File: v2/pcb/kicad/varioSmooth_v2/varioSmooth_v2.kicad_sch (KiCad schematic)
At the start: 1 part, among them U1 MDBT50Q-1MV2

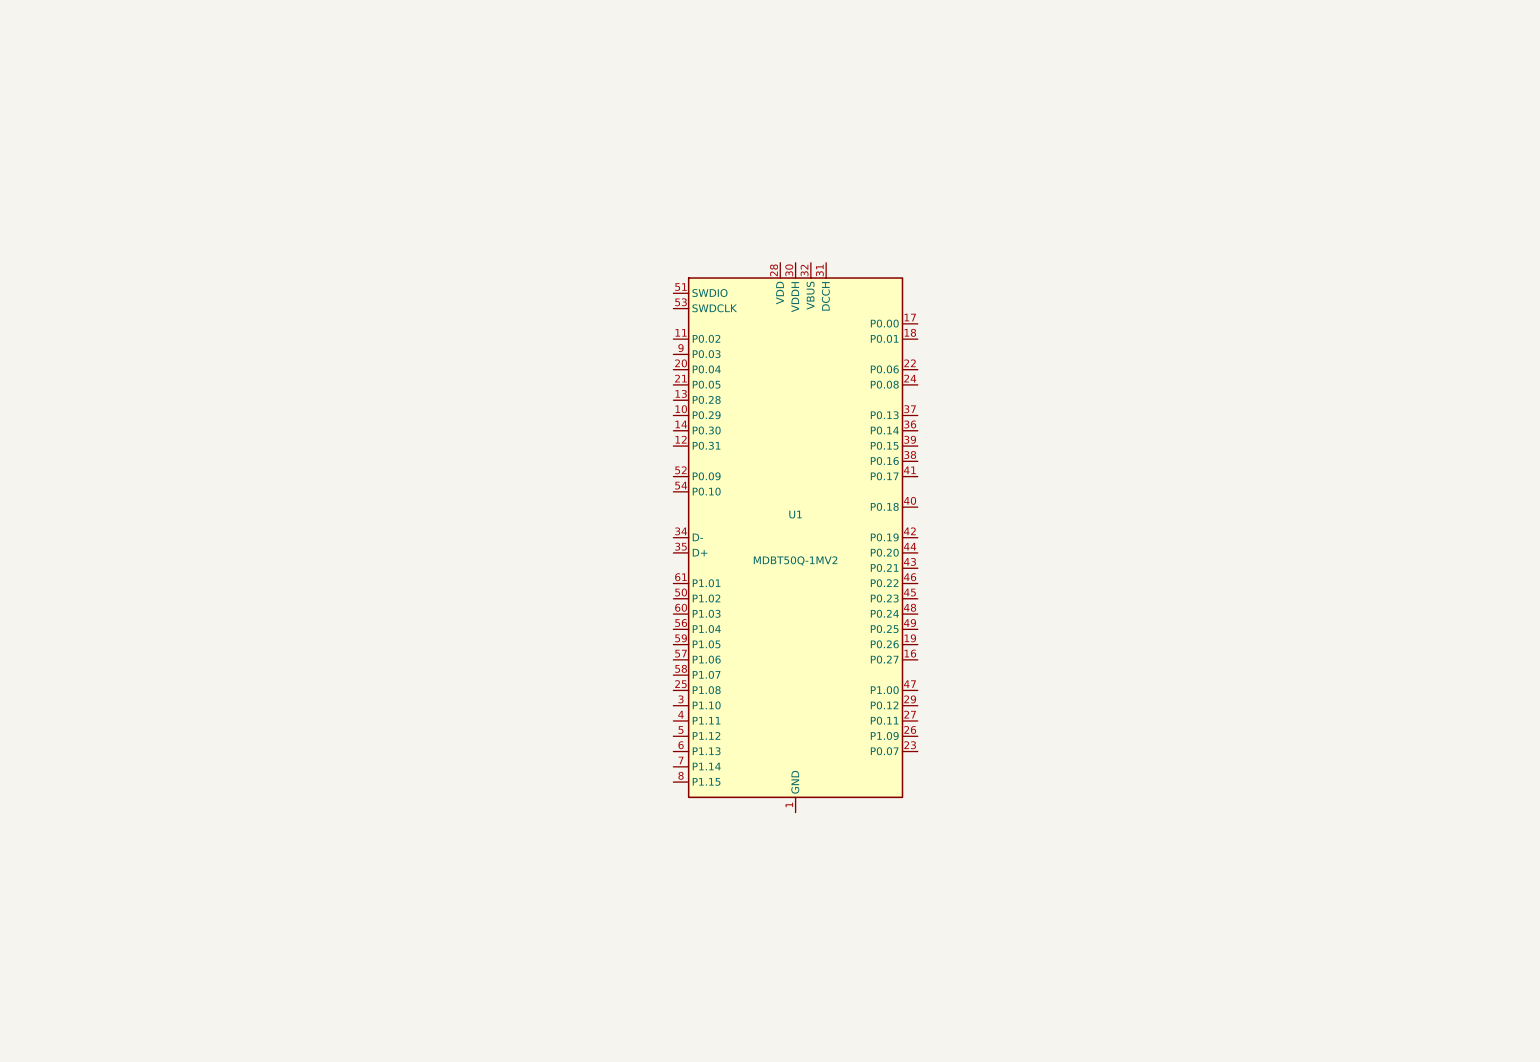
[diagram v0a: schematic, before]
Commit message: Draw the v2 schematic: power, USB, sensor, audio and debug
  LTC4071 shunt charger fed by the solar cells and by USB VBUS through
  Schottky diodes; MDBT50Q in high voltage mode (VDDH from the battery,
  REG0 DC/DC to a 3.3 V VDD). USB-C with CC pull-downs and USBLC6 ESD
  protection, MS5611 on I2C, piezo, button and 32 kHz crystal on the
  Feather pins so the firmware is unchanged, SWD and reset test pads.
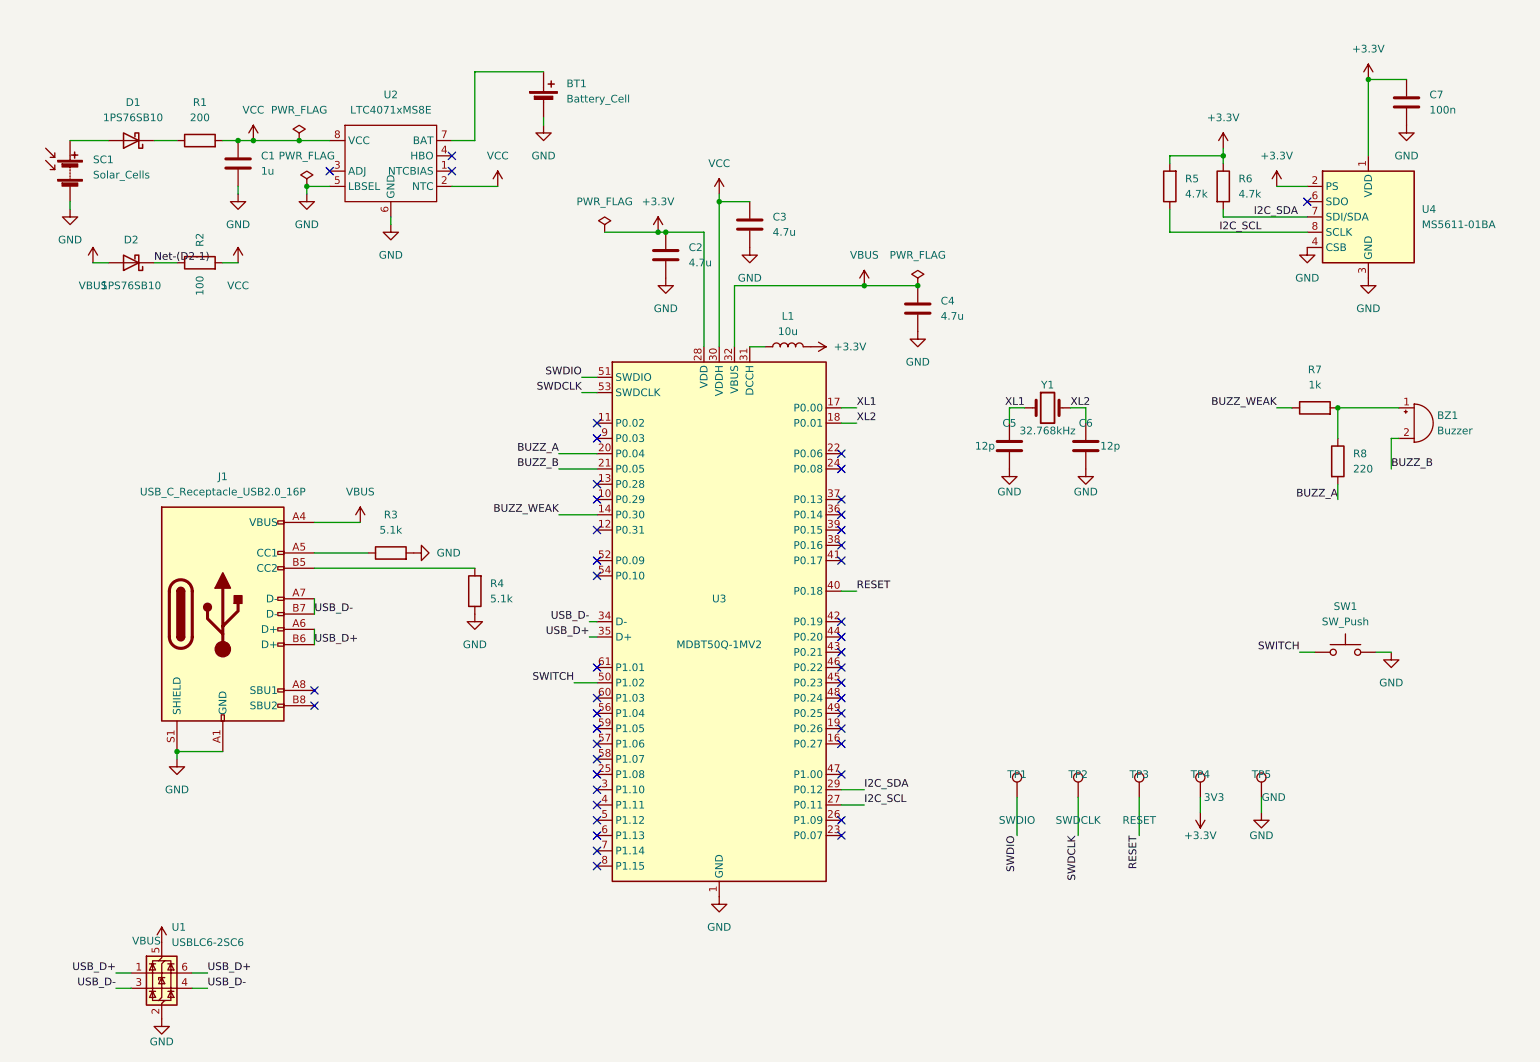
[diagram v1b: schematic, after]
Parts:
- added BT1: Battery_Cell, symbol Device:Battery_Cell
- added BZ1: Buzzer, symbol Device:Buzzer
- added C1: 1u, Capacitor_SMD:C_0603_1608Metric, symbol Device:C
- added C2, C3, C4: 4.7u, Capacitor_SMD:C_0603_1608Metric, symbol Device:C
- added C5, C6: 12p, Capacitor_SMD:C_0603_1608Metric, symbol Device:C
- added C7: 100n, Capacitor_SMD:C_0603_1608Metric, symbol Device:C
- added D1, D2: 1PS76SB10, Diode_SMD:D_SOD-323, symbol Device:D_Schottky
- added J1: USB_C_Receptacle_USB2.0_16P, Connector_USB:USB_C_Receptacle_GCT_USB4105-xx-A_16P_TopMnt_Horizontal, symbol Connector:USB_C_Receptacle_USB2.0_16P
- added L1: 10u, Inductor_SMD:L_0603_1608Metric, symbol Device:L
- added R1: 200, Resistor_SMD:R_0603_1608Metric, symbol Device:R
- added R2: 100, Resistor_SMD:R_0603_1608Metric, symbol Device:R
- added R3, R4: 5.1k, Resistor_SMD:R_0603_1608Metric, symbol Device:R
- added R5, R6: 4.7k, Resistor_SMD:R_0603_1608Metric, symbol Device:R
- added R7: 1k, Resistor_SMD:R_0603_1608Metric, symbol Device:R
- added R8: 220, Resistor_SMD:R_0603_1608Metric, symbol Device:R
- added SC1: Solar_Cells, symbol Device:Solar_Cells
- added SW1: SW_Push, symbol Switch:SW_Push
- added TP1: SWDIO, TestPoint:TestPoint_Pad_D1.5mm, symbol Connector:TestPoint
- added TP2: SWDCLK, TestPoint:TestPoint_Pad_D1.5mm, symbol Connector:TestPoint
- added TP3: RESET, TestPoint:TestPoint_Pad_D1.5mm, symbol Connector:TestPoint
- added TP4: 3V3, TestPoint:TestPoint_Pad_D1.5mm, symbol Connector:TestPoint
- added TP5: GND, TestPoint:TestPoint_Pad_D1.5mm, symbol Connector:TestPoint
- added U1: USBLC6-2SC6, Package_TO_SOT_SMD:SOT-23-6, symbol Power_Protection:USBLC6-2SC6
- added U2: LTC4071xMS8E, Package_SO:MSOP-8-1EP_3x3mm_P0.65mm_EP1.68x1.88mm, symbol varioSmooth_v2:LTC4071xMS8E
- added U4: MS5611-01BA, Package_LGA:LGA-8_3x5mm_P1.25mm, symbol Sensor_Pressure:MS5611-01BA
- added Y1: 32.768kHz, Crystal:Crystal_SMD_3215-2Pin_3.2x1.5mm, symbol Device:Crystal
- renumbered U1 to U3
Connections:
- net GND: now reaches U3.1 (GND), U3.15 (GND), U3.2 (GND), U3.33 (GND), U3.55 (GND)
- net GND: now also BT1.2 (-), C1.2, C2.2, C3.2, C4.2, C5.2, C6.2, C7.2, J1.A1 (GND), J1.A12 (GND), J1.B1 (GND), J1.B12 (GND), J1.S1 (SHIELD), R3.2, R4.1, SC1.2 (-), SW1.2, TP5.1, U1.2 (GND), U2.5 (LBSEL), U2.6 (GND), U2.9 (GND), U4.3 (GND), U4.4 (CSB), U4.5 (CSB)
- net BUZZ_WEAK: now reaches U3.14 (P0.30)
- net BUZZ_WEAK: now also R7.1
- net XL1: now reaches U3.17 (P0.00)
- net XL1: now also C5.1, Y1.1
- net XL2: now reaches U3.18 (P0.01)
- net XL2: now also C6.1, Y1.2
- net BUZZ_A: now reaches U3.20 (P0.04)
- net BUZZ_A: now also R8.2
- net BUZZ_B: now reaches U3.21 (P0.05)
- net BUZZ_B: now also BZ1.2 (-)
- net I2C_SCL: now reaches U3.27 (P0.11)
- net I2C_SCL: now also R5.1, U4.8 (SCLK)
- net +3.3V: now reaches U3.28 (VDD)
- net +3.3V: now also C2.1, C7.1, L1.2, R5.2, R6.1, TP4.1, U4.1 (VDD), U4.2 (PS)
- net I2C_SDA: now reaches U3.29 (P0.12)
- net I2C_SDA: now also R6.2, U4.7 (SDI/SDA)
- net VCC: now reaches U3.30 (VDDH)
- net VCC: now also C1.1, C3.1, R1.2, R2.2, U2.2 (NTC), U2.8 (VCC)
- net at U3.31 (DCCH): now also L1.1
- net VBUS: now reaches U3.32 (VBUS)
- net VBUS: now also C4.1, D2.2 (A), J1.A4 (VBUS), J1.A9 (VBUS), J1.B4 (VBUS), J1.B9 (VBUS), U1.5 (VBUS)
- net USB_D-: now reaches U3.34 (D-)
- net USB_D-: now also J1.A7 (D-), J1.B7 (D-), U1.3 (I/O2), U1.4 (I/O2)
- net USB_D+: now reaches U3.35 (D+)
- net USB_D+: now also J1.A6 (D+), J1.B6 (D+), U1.1 (I/O1), U1.6 (I/O1)
- net RESET: now reaches U3.40 (P0.18)
- net RESET: now also TP3.1
- net SWITCH: now reaches U3.50 (P1.02)
- net SWITCH: now also SW1.1
- net SWDIO: now reaches U3.51 (SWDIO)
- net SWDIO: now also TP1.1
- net SWDCLK: now reaches U3.53 (SWDCLK)
- net SWDCLK: now also TP2.1
- new net: BZ1.1 (+), R7.2, R8.1
- new net: J1.B5 (CC2), R4.2
- new net: D1.1 (K), R1.1
- new net: BT1.1 (+), U2.7 (BAT)
- new net: D1.2 (A), SC1.1 (+)
- new net: J1.A5 (CC1), R3.1
- new net Net-(D2-1): D2.1 (K), R2.1
- no-connect marks 0 -> 45
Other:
- moved on the sheet: U3

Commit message: Split the project into a cockpit extension and a helmet vario
  The in-helmet vario piles up conflicting constraints (BLE antenna, small
  battery, wires through the vents). Plan two devices instead: a phone
  extension for the cockpit with GNSS and IGC backup logging, built on the
  current schematic, then a minimal vario in a small box on a helmet strap.

  The schematic so far: LTC4071 charger, MDBT50Q in high voltage mode,
  USB-C with ESD protection, MS5611, piezo, button, 32 kHz crystal and
  SWD pads, with SMD wire pads for the off-board parts.
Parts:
- BT1, SC1, SW1: footprint (none) -> varioSmooth_v2:WirePad_1x02_SMD_P2.54mm
- BZ1: value Buzzer -> KPEG006; footprint (none) -> varioSmooth_v2:WirePad_1x02_SMD_P2.54mm
- L1: MPN LQM18PN100 -> LQM18DN100M70L
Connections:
- net Net-(D2-1): no longer names the net of D2.1 (K), R2.1
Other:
- note added: "ALIMENTATION - charge solaire et USB (LTC4071, shunt 4,1 V, coupure 3,2 V)"
- note added: "BOUTON DEPORTE (volume / marche-arret)"
- note added: "CAPTEUR DE PRESSION MS5611 (I2C, adresse 0x77)"
- note added: "MODULE BLE nRF52840 (MDBT50Q)"
- note added: "Mode haute tension : VDDH = batterie, REG0 DC/DC -> VDD 3,3 V"
- note added: "PIEZO KPEG006 (3 volumes)"
- note added: "PROGRAMMATION SWD (pastilles de test)"
- note added: "PROTECTION ESD USB (au plus pres de J1)"
- note added: "QUARTZ 32,768 kHz (LFXO)"
- note added: "USB-C (USB 2.0, CC 5,1k = device)"
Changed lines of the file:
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@@
 		(rev "0.1")
 	)
+	(text "PROTECTION ESD USB (au plus pres de J1)"
+		(exclude_from_sim no)
+		(at 42.672 164.084 0)
+		(effects
+			(font
+				(size 1.27 1.27)
+			)
+		)
+	)
+	(text "Mode haute tension : VDDH = batterie, REG0 DC/DC -> VDD 3,3 V"
+		(exclude_from_sim no)
+		(at 159.766 37.338 0)
+		(effects
+			(font
+				(size 1.27 1.27)
+			)
+		)
+	)
+	(text "MODULE BLE nRF52840 (MDBT50Q)"
+		(exclude_from_sim no)
+		(at 159.766 33.528 0)
+		(effects
+			(font
+				(size 1.27 1.27)
+			)
+		)
+	)
+	(text "QUARTZ 32,768 kHz (LFXO)"
+		(exclude_from_sim no)
+		(at 190.5 74.93 0)
+		(effects
+			(font
+				(size 1.27 1.27)
+			)
+		)
+	)
+	(text "BOUTON DEPORTE (volume / marche-arret)"
+		(exclude_from_sim no)
+		(at 226.06 113.03 0)
+		(effects
+			(font
+				(size 1.27 1.27)
+			)
+		)
+	)
+	(text "ALIMENTATION - charge solaire et USB (LTC4071, shunt 4,1 V, coupure 3,2 V)"
+		(exclude_from_sim no)
+		(at 67.31 20.32 0)
+		(effects
+			(font
+				(size 1.27 1.27)
+			)
+		)
+	)
+	(text "CAPTEUR DE PRESSION MS5611 (I2C, adresse 0x77)"
+		(exclude_from_sim no)
+		(at 241.3 18.288 0)
+		(effects
+			(font
+				(size 1.27 1.27)
+			)
+		)
+	)
+	(text "USB-C (USB 2.0, CC 5,1k = device)"
+		(exclude_from_sim no)
+		(at 40.64 91.44 0)
+		(effects
+			(font
+				(size 1.27 1.27)
+			)
+		)
+	)
+	(text "PROGRAMMATION SWD (pastilles de test)"
+		(exclude_from_sim no)
+		(at 205.74 135.89 0)
+		(effects
+			(font
+				(size 1.27 1.27)
+			)
+		)
+	)
+	(text "PIEZO KPEG006 (3 volumes)"
+		(exclude_from_sim no)
+		(at 223.52 72.39 0)
+		(effects
+			(font
+				(size 1.27 1.27)
+			)
+		)
+	)
 	(junction
 		(at 160.02 62.23)
@@
 		)
 	)
-	(label "Net-(D2-1)"
-		(at 41.91 58.42 0)
-		(effects
-			(font
-				(size 1.27 1.27)
-			)
-			(justify left bottom)
-		)
-	)
 	(label "XL2"
 		(at 158.75 85.09 0)
@@
 			)
 		)
-		(property "Footprint" ""
+		(property "Footprint" "varioSmooth_v2:WirePad_1x02_SMD_P2.54mm"
 			(at 240.03 118.11 0)
 			(hide yes)
@@
 		)
 		(property "Value" "VBUS"
-			(at 31.75 62.23 0)
+			(at 31.496 59.944 0)
 			(show_name no)
 			(do_not_autoplace no)
@@
 			)
 		)
-		(property "MPN" "LQM18PN100"
+		(property "MPN" "LQM18DN100M70L"
 			(at 147.32 72.39 90)
 			(hide yes)
@@
 			)
 		)
-		(property "Footprint" ""
+		(property "Footprint" "varioSmooth_v2:WirePad_1x02_SMD_P2.54mm"
 			(at 106.68 30.226 90)
 			(hide yes)
@@
 			)
 		)
-		(property "Value" "Buzzer"
+		(property "Value" "KPEG006"
 			(at 255.27 86.3599 0)
 			(show_name no)
@@
 			)
 		)
-		(property "Footprint" ""
+		(property "Footprint" "varioSmooth_v2:WirePad_1x02_SMD_P2.54mm"
 			(at 250.825 82.55 90)
 			(hide yes)
@@
 			)
 		)
-		(property "Footprint" ""
+		(property "Footprint" "varioSmooth_v2:WirePad_1x02_SMD_P2.54mm"
 			(at 27.94 41.656 90)
 			(hide yes)
@@
 		)
 	)
+	(symbol_instances
+		(path "/5018f1df-9e1e-402d-a847-3df19d33240e/bb335c7b-3b4b-4172-9c29-bc7d96f5974c"
+			(reference "SC1")
+			(unit 1)
+			(value "Solar_Cells")
+			(footprint "varioSmooth_v2:WirePad_1x02_SMD_P2.54mm")
+		)
+		(path "/5018f1df-9e1e-402d-a847-3df19d33240e/9371741f-307a-4b8c-8384-d988d8845f26"
+			(reference "BT1")
+			(unit 1)
+			(value "Battery_Cell")
+			(footprint "varioSmooth_v2:WirePad_1x02_SMD_P2.54mm")
+		)
+		(path "/5018f1df-9e1e-402d-a847-3df19d33240e/943620be-61ad-468e-9f0a-41894943cd5b"
+			(reference "BZ1")
+			(unit 1)
+			(value "KPEG006")
+			(footprint "varioSmooth_v2:WirePad_1x02_SMD_P2.54mm")
+		)
+		(path "/5018f1df-9e1e-402d-a847-3df19d33240e/3f40cdba-f7e2-46d2-a2a0-b4c0d905c870"
+			(reference "SW1")
+			(unit 1)
+			(value "SW_Push")
+			(footprint "varioSmooth_v2:WirePad_1x02_SMD_P2.54mm")
+		)
+)
 	(sheet_instances
 		(path "/"

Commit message: Place and route the v2 helmet vario PCB
  Two-layer 20 x 32.75 mm board, single-sided assembly. The MDBT50Q antenna
  sits flush with the top edge and the USB-C receptacle at the bottom.
  Wire pads (solar cells, battery, buzzer, button) and the SWD/RESET/3V3/GND
  test pads are on the back.

  Routing was done by hand: the 32 kHz crystal next to the module, the
  VDDH/DCCH/L1 loop under it, USB D+/D- through the USBLC6 flow-through
  pads, then power, I2C, buzzer and SWD. GND pours cover both layers with
  stitching vias. The remaining DRC errors come from the USB-C footprint
  itself (hole clearance, starved thermals on A1/B12).

  Board rules: 0.15 mm minimum track, 0.3 mm edge clearance, 0.2 mm hole
  clearance.

  Add LCSC part numbers for JLCPCB assembly; U2 (LTC4071) stays
  hand-soldered.

  This USB version is kept as the development prototype; the compact
  helmet board without USB comes next.
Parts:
- C1: LCSC (none) -> C15849
- C2, C3, C4: LCSC (none) -> C19666
- C5, C6: LCSC (none) -> C38523
- C7: LCSC (none) -> C14663
- D1, D2: LCSC (none) -> C551397
- J1: LCSC (none) -> C3020560
- L1: LCSC (none) -> C713281
- R1: LCSC (none) -> C8218
- R2: LCSC (none) -> C22775
- R3, R4: LCSC (none) -> C23186
- R5, R6: LCSC (none) -> C23162
- R7: LCSC (none) -> C21190
- R8: LCSC (none) -> C22962
- U1: LCSC (none) -> C7519
- U2: DNP (none) -> hand-soldered, not assembled by JLCPCB
- U3: LCSC (none) -> C5118826
- U4: LCSC (none) -> C37148
- Y1: LCSC (none) -> C99010
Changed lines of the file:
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@@
 			)
 		)
+		(property "LCSC" "C37148"
+	(id 0)
+	(at 243.84 50.8 0)
+	(effects
+		(font
+			(size 1.27 1.27)
+		)
+		(hide yes)
+	)
+)
 		(pin "1"
 		)
@@
 			)
 		)
+		(property "LCSC" "C38523"
+	(id 0)
+	(at 196.85 88.9 0)
+	(effects
+		(font
+			(size 1.27 1.27)
+		)
+		(hide yes)
+	)
+)
 		(pin "1"
 		)
@@
 			)
 		)
+		(property "LCSC" "C23162"
+	(id 0)
+	(at 219.71 45.72 0)
+	(effects
+		(font
+			(size 1.27 1.27)
+		)
+		(hide yes)
+	)
+)
 		(pin "2"
 		)
@@
 			)
 		)
+		(property "LCSC" "C7519"
+	(id 0)
+	(at 43.18 176.53 0)
+	(effects
+		(font
+			(size 1.27 1.27)
+		)
+		(hide yes)
+	)
+)
 		(pin "1"
 		)
@@
 			)
 		)
+		(property "LCSC" "C14663"
+	(id 0)
+	(at 250.19 31.75 0)
+	(effects
+		(font
+			(size 1.27 1.27)
+		)
+		(hide yes)
+	)
+)
 		(pin "2"
 		)
@@
 			)
 		)
+		(property "LCSC" "C5118826"
+	(id 0)
+	(at 135.89 118.11 0)
+	(effects
+		(font
+			(size 1.27 1.27)
+		)
+		(hide yes)
+	)
+)
 		(pin "1"
 		)
@@
 			)
 		)
+		(property "LCSC" "C19666"
+	(id 0)
+	(at 127 57.15 0)
+	(effects
+		(font
+			(size 1.27 1.27)
+		)
+		(hide yes)
+	)
+)
 		(pin "2"
 		)
@@
 			)
 		)
+		(property "LCSC" "C99010"
+	(id 0)
+	(at 190.5 82.55 0)
+	(effects
+		(font
+			(size 1.27 1.27)
+		)
+		(hide yes)
+	)
+)
 		(pin "1"
 		)
@@
 			)
 		)
+		(property "LCSC" "C38523"
+	(id 0)
+	(at 184.15 88.9 0)
+	(effects
+		(font
+			(size 1.27 1.27)
+		)
+		(hide yes)
+	)
+)
 		(pin "1"
 		)
@@
 			)
 		)
+		(property "LCSC" "C22775"
+	(id 0)
+	(at 49.53 58.42 0)
+	(effects
+		(font
+			(size 1.27 1.27)
+		)
+		(hide yes)
+	)
+)
 		(pin "1"
 		)
@@
 			)
 		)
+		(property "LCSC" "C713281"
+	(id 0)
+	(at 147.32 72.39 0)
+	(effects
+		(font
+			(size 1.27 1.27)
+		)
+		(hide yes)
+	)
+)
 		(pin "1"
 		)
@@
 			)
 		)
+		(property "LCSC" "C21190"
+	(id 0)
+	(at 234.95 82.55 0)
+	(effects
+		(font
+			(size 1.27 1.27)
+		)
+		(hide yes)
+	)
+)
 		(pin "2"
 		)
@@
 			)
 		)
+		(property "LCSC" "C22962"
+	(id 0)
+	(at 238.76 91.44 0)
+	(effects
+		(font
+			(size 1.27 1.27)
+		)
+		(hide yes)
+	)
+)
 		(pin "2"
 		)
@@
 			)
 		)
+		(property "LCSC" "C23186"
+	(id 0)
+	(at 95.25 113.03 0)
+	(effects
+		(font
+			(size 1.27 1.27)
+		)
+		(hide yes)
+	)
+)
 		(pin "2"
 		)
@@
 			)
 		)
+		(property "LCSC" "C8218"
+	(id 0)
+	(at 49.53 38.1 0)
+	(effects
+		(font
+			(size 1.27 1.27)
+		)
+		(hide yes)
+	)
+)
 		(pin "2"
 		)
@@
 			)
 		)
+		(property "LCSC" "C551397"
+	(id 0)
+	(at 38.1 38.1 0)
+	(effects
+		(font
+			(size 1.27 1.27)
+		)
+		(hide yes)
+	)
+)
 		(pin "2"
 		)
@@
 			)
 		)
+		(property "LCSC" "C23186"
+	(id 0)
+	(at 81.28 106.68 0)
+	(effects
+		(font
+			(size 1.27 1.27)
+		)
+		(hide yes)
+	)
+)
 		(pin "2"
 		)
@@
 			)
 		)
+		(property "LCSC" "C19666"
+	(id 0)
+	(at 168.91 66.04 0)
+	(effects
+		(font
+			(size 1.27 1.27)
+		)
+		(hide yes)
+	)
+)
 		(pin "2"
 		)
@@
 			)
 		)
+		(property "DNP" "hand-soldered, not assembled by JLCPCB"
+	(id 0)
+	(at 81.28 43.18 0)
+	(effects
+		(font
+			(size 1.27 1.27)
+		)
+		(hide yes)
+	)
+)
 		(pin "4"
 		)
@@
 			)
 		)
+		(property "LCSC" "C15849"
+	(id 0)
+	(at 55.88 41.91 0)
+	(effects
+		(font
+			(size 1.27 1.27)
+		)
+		(hide yes)
+	)
+)
 		(pin "2"
 		)
@@
 			)
 		)
+		(property "LCSC" "C551397"
+	(id 0)
+	(at 38.1 58.42 0)
+	(effects
+		(font
+			(size 1.27 1.27)
+		)
+		(hide yes)
+	)
+)
 		(pin "1"
 		)
@@
 			)
 		)
+		(property "LCSC" "C3020560"
+	(id 0)
+	(at 53.34 116.84 0)
+	(effects
+		(font
+			(size 1.27 1.27)
+		)
+		(hide yes)
+	)
+)
 		(pin "B1"
 		)
@@
 			)
 		)
+		(property "LCSC" "C23162"
+	(id 0)
+	(at 210.82 45.72 0)
+	(effects
+		(font
+			(size 1.27 1.27)
+		)
+		(hide yes)
+	)
+)
 		(pin "2"
 		)
@@
 			)
 		)
+		(property "LCSC" "C19666"
+	(id 0)
+	(at 140.97 52.07 0)
+	(effects
+		(font
+			(size 1.27 1.27)
+		)
+		(hide yes)
+	)
+)
 		(pin "2"
 		)
